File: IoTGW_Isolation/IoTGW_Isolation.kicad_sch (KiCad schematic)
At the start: 33 parts, among them J1 39502-1008, J4 39502-1008, Q1 Q_PMOS, U1 TEA1-0505, U2 ISO1452BDWR, U3 LTV-817S, U4 LTV-817S, U5 LTV-817S, U6 LTV-817S, U7 LTV-817S, U8 LTV-817S

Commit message: pcb updates schemartic update
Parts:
- added TP1: LOGO, IoTGW:INSET_LOGO, symbol Connector:TestPoint
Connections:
- no-connect marks 9 -> 10
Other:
- moved on the sheet: Q1, R1

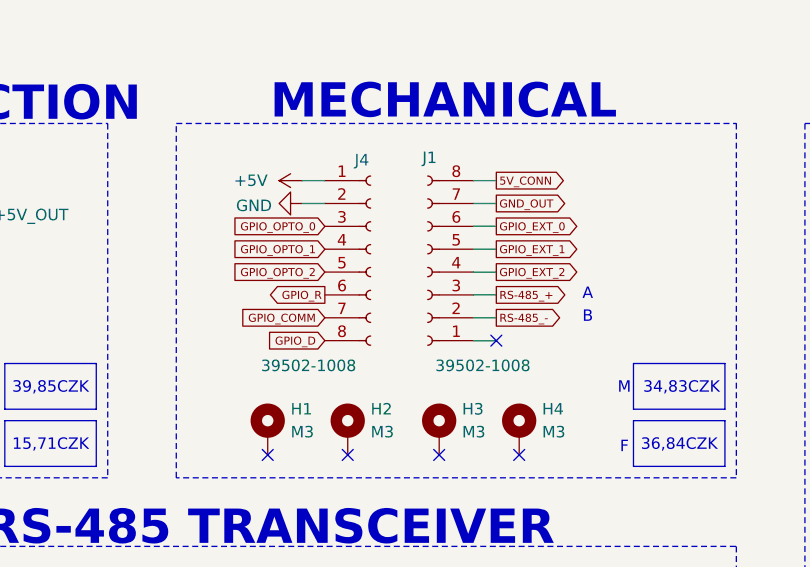
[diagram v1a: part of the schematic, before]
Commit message: smaller PCB
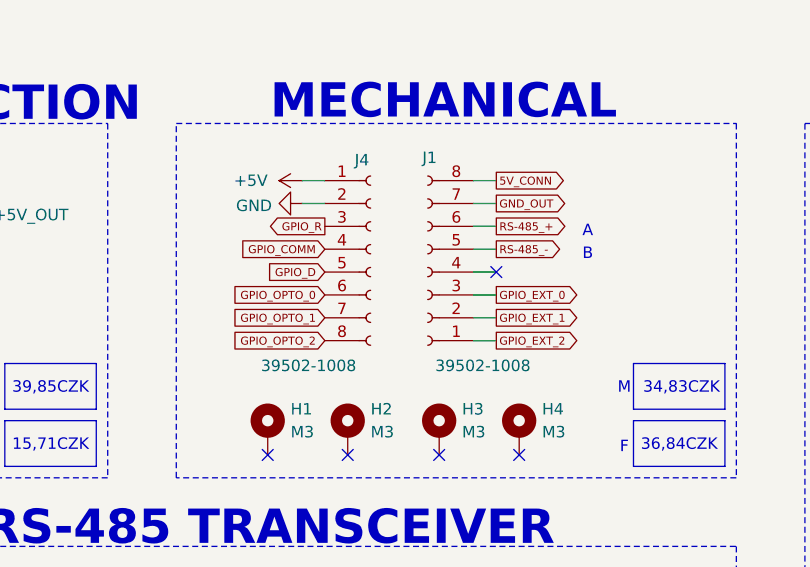
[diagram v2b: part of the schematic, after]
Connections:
- net GPIO_COMM: now also J4.4 (Pin_4); no longer J4.7 (Pin_7)
- net GPIO_D: now also J4.5 (Pin_5); no longer J4.8 (Pin_8)
- net GPIO_EXT_0: now also J1.3 (Pin_3); no longer J1.6 (Pin_6)
- net GPIO_EXT_1: now also J1.2 (Pin_2); no longer J1.5 (Pin_5)
- net GPIO_EXT_2: now also J1.1 (Pin_1); no longer J1.4 (Pin_4)
- net GPIO_OPTO_0: now also J4.6 (Pin_6); no longer J4.3 (Pin_3)
- net GPIO_OPTO_1: now also J4.7 (Pin_7); no longer J4.4 (Pin_4)
- net GPIO_OPTO_2: now also J4.8 (Pin_8); no longer J4.5 (Pin_5)
- net GPIO_R: now also J4.3 (Pin_3); no longer J4.6 (Pin_6)
- net RS-485_+: now also J1.6 (Pin_6); no longer J1.3 (Pin_3)
- net RS-485_-: now also J1.5 (Pin_5); no longer J1.2 (Pin_2)

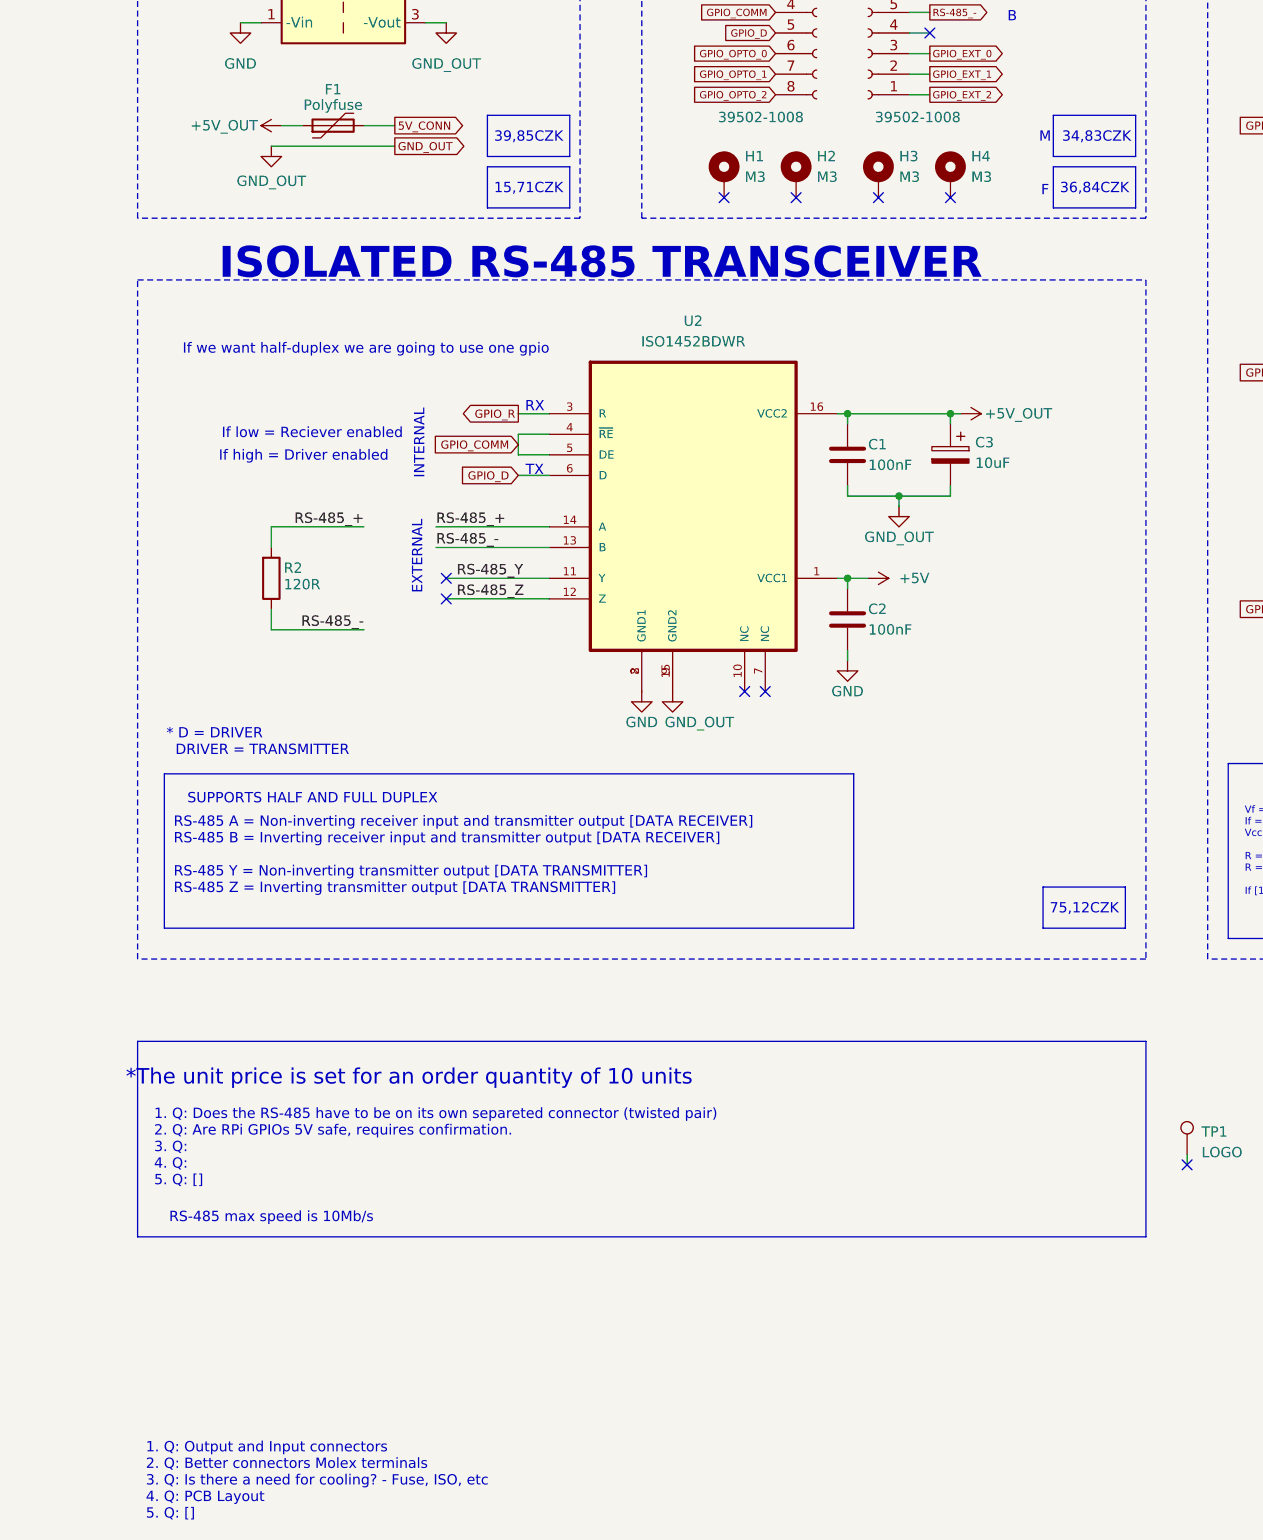
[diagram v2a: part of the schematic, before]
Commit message: to do list 3.3v logic update
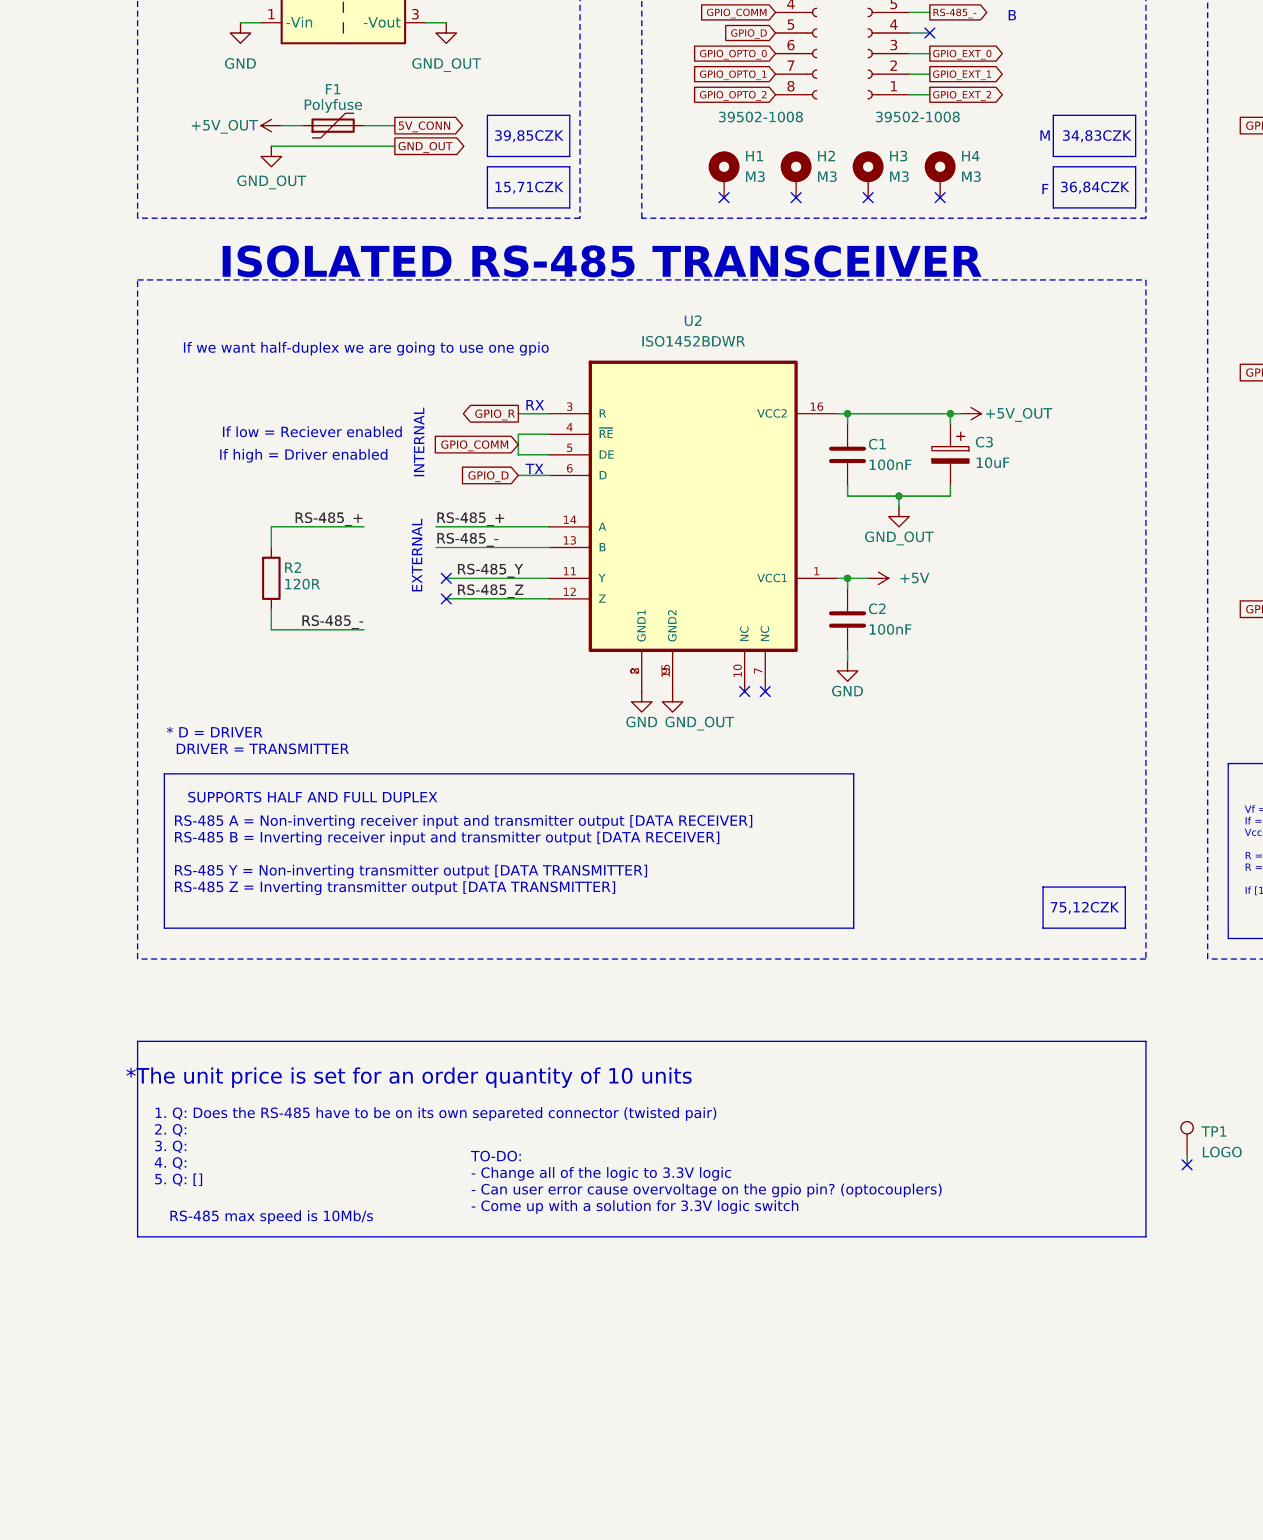
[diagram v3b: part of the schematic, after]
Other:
- note added: "1. Q: Does the RS-485 have to be on its own separeted connector (twisted pair) 2. Q: 3. Q: 4. Q: 5. Q: []"
- note added: "TO-DO: - Change all of the logic to 3.3V logic - Can user error cause overvoltage on the gpio pin? (optocouplers) - Come up with a solution for 3.3V logic switch"
- note removed: "1. Q: Does the RS-485 have to be on its own separeted connector (twisted pair) 2. Q: Are RPi GPIOs 5V safe, requires confirmation. 3. Q: 4. Q: 5. Q: []"
- note removed: "1. Q: Output and Input connectors 2. Q: Better connectors Molex terminals 3. Q: Is there a need for cooling? - Fuse, ISO, etc 4. Q: PCB Layout 5. Q: []"
- moved on the sheet: H3, H4
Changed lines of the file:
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@@
 	)
 	(no_connect
-		(at 123.19 62.23)
+		(at 121.92 62.23)
 	)
 	(no_connect
@@
 	)
 	(no_connect
-		(at 114.3 62.23)
+		(at 113.03 62.23)
 	)
 	(no_connect
@@
 		)
 	)
-	(text "1. Q: Output and Input connectors\n2. Q: Better connectors Molex terminals\n3. Q: Is there a need for cooling? - Fuse, ISO, etc\n4. Q: PCB Layout\n5. Q: []"
+	(text "TO-DO:\n- Change all of the logic to 3.3V logic\n- Can user error cause overvoltage on the gpio pin? (optocouplers)\n- Come up with a solution for 3.3V logic switch"
 		(exclude_from_sim no)
-		(at 23.876 220.726 0)
+		(at 64.008 183.896 0)
 		(effects
 			(font
@@
 		)
 	)
-	(text "1. Q: Does the RS-485 have to be on its own separeted connector (twisted pair)\n2. Q: Are RPi GPIOs 5V safe, requires confirmation.\n3. Q: \n4. Q: \n5. Q: []"
+	(text "1. Q: Does the RS-485 have to be on its own separeted connector (twisted pair)\n2. Q: \n3. Q: \n4. Q: \n5. Q: []"
 		(exclude_from_sim no)
 		(at 24.892 179.578 0)
@@
 	(symbol
 		(lib_id "Mechanical:MountingHole_Pad")
-		(at 123.19 59.69 0)
+		(at 121.92 59.69 0)
 		(unit 1)
 		(exclude_from_sim yes)
@@
 		(fields_autoplaced yes)
 		(property "Reference" "H4"
-			(at 125.73 57.1499 0)
+			(at 124.46 57.1499 0)
 			(effects
 				(font
@@
 		)
 		(property "Value" "M3"
-			(at 125.73 59.6899 0)
+			(at 124.46 59.6899 0)
 			(effects
 				(font
@@
 		)
 		(property "Footprint" "MountingHole:MountingHole_3.2mm_M3_Pad_Via"
-			(at 123.19 59.69 0)
+			(at 121.92 59.69 0)
 			(effects
 				(font
@@
 		)
 		(property "Datasheet" "~"
-			(at 123.19 59.69 0)
+			(at 121.92 59.69 0)
 			(effects
 				(font
@@
 		)
 		(property "Description" "Mounting Hole with connection"
-			(at 123.19 59.69 0)
+			(at 121.92 59.69 0)
 			(effects
 				(font
@@
 	(symbol
 		(lib_id "Mechanical:MountingHole_Pad")
-		(at 114.3 59.69 0)
+		(at 113.03 59.69 0)
 		(unit 1)
 		(exclude_from_sim yes)
@@
 		(fields_autoplaced yes)
 		(property "Reference" "H3"
-			(at 116.84 57.1499 0)
+			(at 115.57 57.1499 0)
 			(effects
 				(font
@@
 		)
 		(property "Value" "M3"
-			(at 116.84 59.6899 0)
+			(at 115.57 59.6899 0)
 			(effects
 				(font
@@
 		)
 		(property "Footprint" "MountingHole:MountingHole_3.2mm_M3_Pad_Via"
-			(at 114.3 59.69 0)
+			(at 113.03 59.69 0)
 			(effects
 				(font
@@
 		)
 		(property "Datasheet" "~"
-			(at 114.3 59.69 0)
+			(at 113.03 59.69 0)
 			(effects
 				(font
@@
 		)
 		(property "Description" "Mounting Hole with connection"
-			(at 114.3 59.69 0)
+			(at 113.03 59.69 0)
 			(effects
 				(font

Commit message: schematic update 3.3V logic
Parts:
- removed J1, J4: 39502-1008, IoTGW:Molex_8pin_3.50, symbol Connector:Conn_01x08_Socket
- added C? (x2): 10uF, Capacitor_Tantalum_SMD:CP_EIA-3216-18_Kemet-A_Pad1.58x1.35mm_HandSolder, symbol Device:C_Polarized
- added F2: Polyfuse, Fuse:Fuse_0805_2012Metric, symbol Device:Polyfuse
- added J1, J2: 39502-1009, IoTGW:Molex_9pin_3.50, symbol Connector:Conn_01x09_Socket
- added U?: NCP1117-3.3, Package_TO_SOT_SMD:SOT-223-3_TabPin2, symbol Regulator_Linear:NCP1117-3.3_SOT223
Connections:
- net +5V: now also J1.2 (Pin_2)
- net +5V_OUT: now also C?.1, F2.1, U?.3 (VI); no longer F1.1
- net 5V_CONN: now also F2.2, J2.2 (Pin_2); no longer F1.2
- net GND: now also J1.3 (Pin_3)
- net GND_OUT: now also C?.2, C?.2, J2.3 (Pin_3), U?.1 (GND)
- net GPIO_COMM: now also J1.5 (Pin_5)
- net GPIO_D: now also J1.6 (Pin_6)
- net GPIO_EXT_0: now also J2.7 (Pin_7)
- net GPIO_EXT_1: now also J2.8 (Pin_8)
- net GPIO_EXT_2: now also J2.9 (Pin_9)
- net GPIO_OPTO_0: now also J1.7 (Pin_7)
- net GPIO_OPTO_1: now also J1.8 (Pin_8)
- net GPIO_OPTO_2: now also J1.9 (Pin_9)
- net GPIO_R: now also J1.4 (Pin_4)
- net RS-485_+: now also J2.4 (Pin_4)
- net RS-485_-: now also J2.5 (Pin_5)
- new net +3.3V: J1.1 (Pin_1)
- new net +3.3V_OUT: C?.1, F1.1, U?.2 (VO)
- new net 3.3V_CONN: F1.2, J2.1 (Pin_1)
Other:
- note added: "CONNECTORS"
- note added: "Isolation: 1.5kV Output current max: 200mA Voltage input: 4.5V-5.5V"
- note added: "LDO. VOLTAGE REG."
- note added: "MOUNTING HOLE"
- note added: "POWER ISOLATION"
- note removed: "A"
- note removed: "B"
- note removed: "MECHANICAL"
- moved on the sheet: C1, C2, C3, F1, H1, H2, H3, H4, R10, R11, R12, R13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

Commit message: 3,3V logic update
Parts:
- gave numbers to parts that had none: 3
- renumbered C1 to C3, C2 to C4, C3 to C5, R11 to R10, R12 to R11, R13 to R12, R14 to R13, R2 to R14, R3 to R2, R4 to R3, R5 to R4, R6 to R5, R7 to R6, R8 to R7, R9 to R8, R10 to R9, U2 to U9
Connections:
- net +3.3V: now also C4.1, R11.2, R12.2, R13.2, U9.1 (VCC1)
- net +3.3V_OUT: now also R5.2, R6.2, R7.2
- net +5V: no longer C4.1, R11.2, R12.2, R13.2, U9.1 (VCC1)
- net +5V_OUT: no longer R5.2, R6.2, R7.2
- net 3.3V_CONN: now also J2.9 (Pin_9); no longer J2.1 (Pin_1)
- net 5V_CONN: now also J2.8 (Pin_8); no longer J2.2 (Pin_2)
- net GND_OUT: now also J2.7 (Pin_7); no longer J2.3 (Pin_3)
- net GPIO_EXT_0: now also J2.3 (Pin_3); no longer J2.7 (Pin_7)
- net GPIO_EXT_1: now also J2.2 (Pin_2); no longer J2.8 (Pin_8)
- net GPIO_EXT_2: now also J2.1 (Pin_1); no longer J2.9 (Pin_9)
- net RS-485_+: now also J2.6 (Pin_6); no longer J2.4 (Pin_4)
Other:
- moved on the sheet: C1, C2, C3, C4, C5, F1, F2, H1, H2, H3, H4, J1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

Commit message: bom update
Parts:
- R10, R2, R3, R4, R8, R9: value 200R -> 110R
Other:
- note added: "Vf = 1.2V If = 20mA Vcc = 3.3V (RPi) R = (Vcc - Vf) / If R = 105R ~ 120R If [120] = 17.5mA"
- moved on the sheet: H1, H2, H3, H4
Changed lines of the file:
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@@
 	)
 	(no_connect
-		(at 336.55 186.69)
+		(at 332.74 185.42)
 	)
 	(no_connect
@@
 	)
 	(no_connect
-		(at 363.22 186.69)
+		(at 359.41 185.42)
 	)
 	(no_connect
@@
 	)
 	(no_connect
-		(at 345.44 186.69)
+		(at 341.63 185.42)
 	)
 	(no_connect
@@
 	)
 	(no_connect
-		(at 354.33 186.69)
+		(at 350.52 185.42)
 	)
 	(no_connect
@@
 		)
 	)
-	(bus
-		(pts
-			(xy 83.82 128.27) (xy 83.82 119.38)
-		)
-		(stroke
-			(width 0)
-			(type default)
-		)
-	)
 	(wire
 		(pts
@@
 		)
 	)
-	(bus
-		(pts
-			(xy 83.82 119.38) (xy 92.71 119.38)
-		)
-		(stroke
-			(width 0)
-			(type default)
-		)
-	)
 	(wire
 		(pts
@@
 		)
 	)
-	(bus
-		(pts
-			(xy 248.92 101.6) (xy 240.03 101.6)
-		)
-		(stroke
-			(width 0)
-			(type default)
-		)
-	)
 	(wire
 		(pts
@@
 		)
 	)
-	(bus
-		(pts
-			(xy 321.31 163.83) (xy 312.42 163.83)
-		)
-		(stroke
-			(width 0)
-			(type default)
-		)
-	)
 	(wire
 		(pts
@@
 		)
 	)
-	(bus
-		(pts
-			(xy 312.42 154.94) (xy 312.42 163.83)
-		)
-		(stroke
-			(width 0)
-			(type default)
-		)
-	)
 	(rectangle
 		(start 96.52 208.788)
-		(end 134.62 230.378)
+		(end 150.495 230.378)
 		(stroke
 			(width 0)
@@
 	(text "Vf = 1.2V\nIf = 20mA\nVcc = 5V (RPi)\n\nR = (Vcc - Vf) / If\nR = 190 ~ 200R\n\nIf [200R] = 19mA"
 		(exclude_from_sim no)
-		(at 114.935 219.71 0)
+		(at 133.985 219.71 0)
 		(effects
 			(font
@@
 		)
 	)
+	(text "Vf = 1.2V\nIf = 20mA\nVcc = 3.3V (RPi)\n\nR = (Vcc - Vf) / If\nR = 105R ~ 120R\n\nIf [120] = 17.5mA"
+		(exclude_from_sim no)
+		(at 116.205 219.71 0)
+		(effects
+			(font
+				(size 0.889 0.889)
+				(color 0 0 0 1)
+			)
+			(justify left)
+		)
+	)
 	(text "If high = Driver enabled"
 		(exclude_from_sim no)
@@
 			)
 		)
-		(property "Value" "200R"
+		(property "Value" "110R"
 			(at 189.23 95.504 90)
 			(effects
@@
 	(symbol
 		(lib_id "Mechanical:MountingHole_Pad")
-		(at 363.22 184.15 0)
+		(at 359.41 182.88 0)
 		(unit 1)
 		(exclude_from_sim yes)
@@
 		(fields_autoplaced yes)
 		(property "Reference" "H4"
-			(at 365.76 181.6099 0)
+			(at 361.95 180.3399 0)
 			(effects
 				(font
@@
 		)
 		(property "Value" "M3"
-			(at 365.76 184.1499 0)
+			(at 361.95 182.8799 0)
 			(effects
 				(font
@@
 		)
 		(property "Footprint" "MountingHole:MountingHole_3.2mm_M3_Pad_Via"
-			(at 363.22 184.15 0)
+			(at 359.41 182.88 0)
 			(effects
 				(font
@@
 		)
 		(property "Datasheet" "~"
-			(at 363.22 184.15 0)
+			(at 359.41 182.88 0)
 			(effects
 				(font
@@
 		)
 		(property "Description" "Mounting Hole with connection"
-			(at 363.22 184.15 0)
+			(at 359.41 182.88 0)
 			(effects
 				(font
@@
 	(symbol
 		(lib_id "Mechanical:MountingHole_Pad")
-		(at 336.55 184.15 0)
+		(at 332.74 182.88 0)
 		(unit 1)
 		(exclude_from_sim yes)
@@
 		(fields_autoplaced yes)
 		(property "Reference" "H1"
-			(at 339.09 181.6099 0)
+			(at 335.28 180.3399 0)
 			(effects
 				(font
@@
 		)
 		(property "Value" "M3"
-			(at 339.09 184.1499 0)
+			(at 335.28 182.8799 0)
 			(effects
 				(font
@@
 		)
 		(property "Footprint" "MountingHole:MountingHole_3.2mm_M3_Pad_Via"
-			(at 336.55 184.15 0)
+			(at 332.74 182.88 0)
 			(effects
 				(font
@@
 		)
 		(property "Datasheet" "~"
-			(at 336.55 184.15 0)
+			(at 332.74 182.88 0)
 			(effects
 				(font
@@
 		)
 		(property "Description" "Mounting Hole with connection"
-			(at 336.55 184.15 0)
+			(at 332.74 182.88 0)
 			(effects
 				(font
@@
 			)
 		)
-		(property "Value" "200R"
+		(property "Value" "110R"
 			(at 121.92 129.794 90)
 			(effects
@@
 			)
 		)
-		(property "Value" "200R"
+		(property "Value" "110R"
 			(at 189.23 164.084 90)
 			(effects
@@
 			)
 		)
-		(property "Value" "200R"
+		(property "Value" "110R"
 			(at 121.92 95.25 90)
 			(effects
@@
 	(symbol
 		(lib_id "Mechanical:MountingHole_Pad")
-		(at 354.33 184.15 0)
+		(at 350.52 182.88 0)
 		(unit 1)
 		(exclude_from_sim yes)
@@
 		(fields_autoplaced yes)
 		(property "Reference" "H3"
-			(at 356.87 181.6099 0)
+			(at 353.06 180.3399 0)
 			(effects
 				(font
@@
 		)
 		(property "Value" "M3"
-			(at 356.87 184.1499 0)
+			(at 353.06 182.8799 0)
 			(effects
 				(font
@@
 		)
 		(property "Footprint" "MountingHole:MountingHole_3.2mm_M3_Pad_Via"
-			(at 354.33 184.15 0)
+			(at 350.52 182.88 0)
 			(effects
 				(font
@@
 		)
 		(property "Datasheet" "~"
-			(at 354.33 184.15 0)
+			(at 350.52 182.88 0)
 			(effects
 				(font
@@
 		)
 		(property "Description" "Mounting Hole with connection"
-			(at 354.33 184.15 0)
+			(at 350.52 182.88 0)
 			(effects
 				(font
@@
 			)
 		)
-		(property "Value" "200R"
+		(property "Value" "110R"
 			(at 189.23 129.794 90)
 			(effects
@@
 	(symbol
 		(lib_id "Mechanical:MountingHole_Pad")
-		(at 345.44 184.15 0)
+		(at 341.63 182.88 0)
 		(unit 1)
 		(exclude_from_sim yes)
@@
 		(fields_autoplaced yes)
 		(property "Reference" "H2"
-			(at 347.98 181.6099 0)
+			(at 344.17 180.3399 0)
 			(effects
 				(font
@@
 		)
 		(property "Value" "M3"
-			(at 347.98 184.1499 0)
+			(at 344.17 182.8799 0)
 			(effects
 				(font
@@
 		)
 		(property "Footprint" "MountingHole:MountingHole_3.2mm_M3_Pad_Via"
-			(at 345.44 184.15 0)
+			(at 341.63 182.88 0)
 			(effects
 				(font
@@
 		)
 		(property "Datasheet" "~"
-			(at 345.44 184.15 0)
+			(at 341.63 182.88 0)
 			(effects
 				(font
@@
 		)
 		(property "Description" "Mounting Hole with connection"
-			(at 345.44 184.15 0)
+			(at 341.63 182.88 0)
 			(effects
 				(font
@@
 			)
 		)
-		(property "Value" "200R"
+		(property "Value" "110R"
 			(at 121.92 164.084 90)
 			(effects
